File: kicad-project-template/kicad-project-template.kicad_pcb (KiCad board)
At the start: 2 copper layers, 25 x 25 mm, 1 part

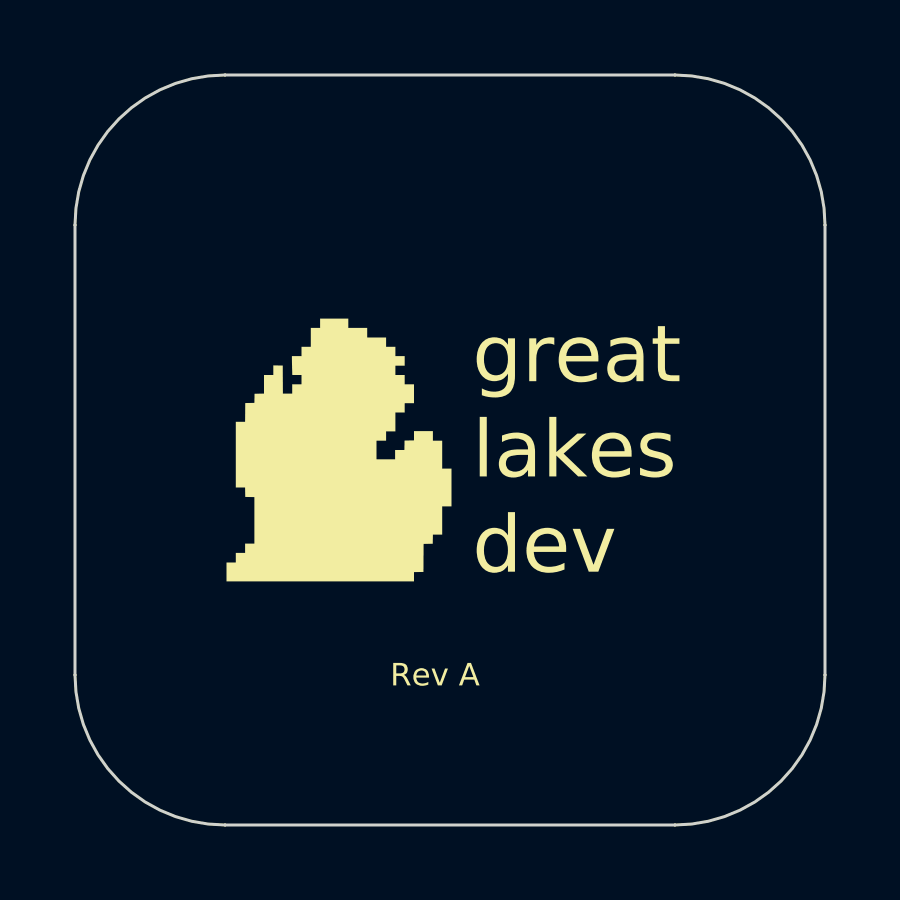
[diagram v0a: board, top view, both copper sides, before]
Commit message: Updated logos and sheet naming to everyday dev
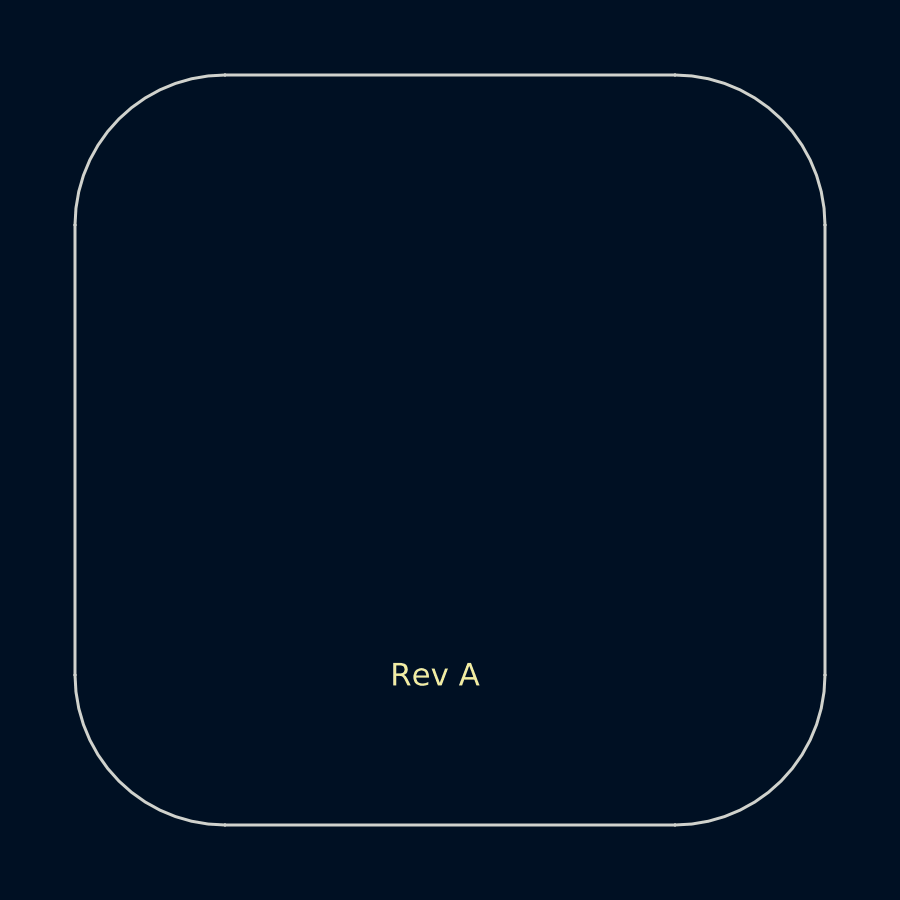
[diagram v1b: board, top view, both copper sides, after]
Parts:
- removed the G*** at (108.8, 97.5)
- added G***: LOGO, gld:edd-logo, F.Cu at (112.3, 96.9)

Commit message: Added manufacturer to bom output and updated MFP to MPN to follow other standards
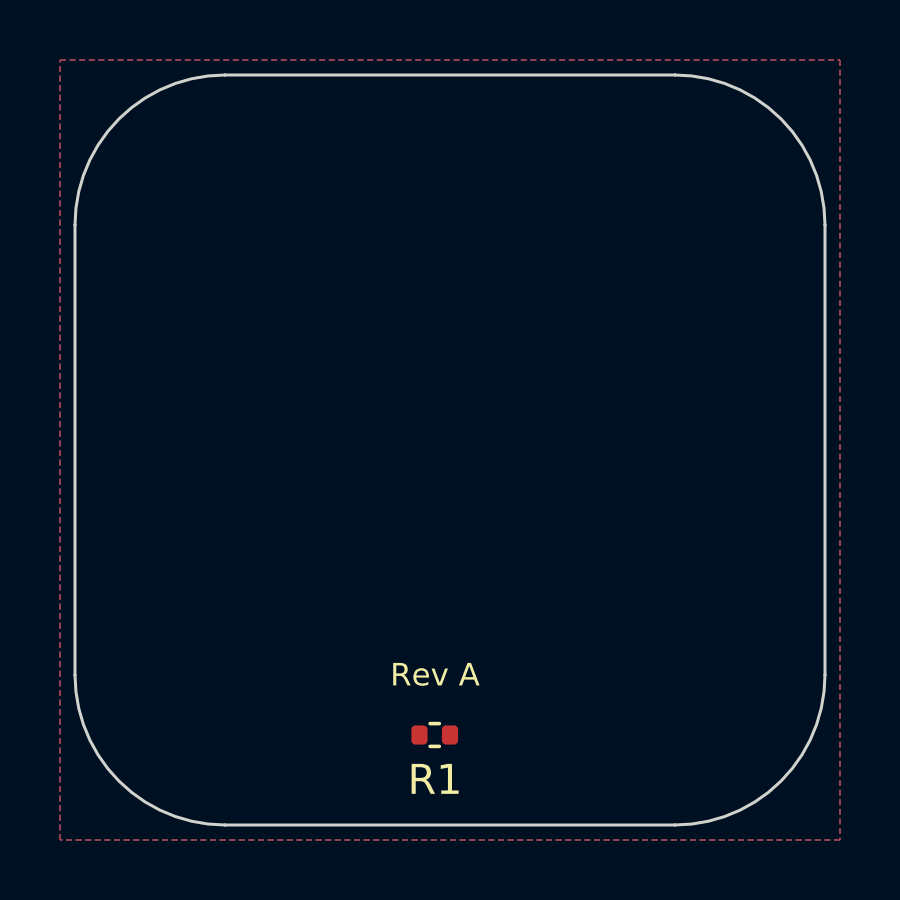
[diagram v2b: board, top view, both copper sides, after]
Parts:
- added R1: 10k, Resistor_SMD:R_0402_1005Metric, F.Cu at (112.0, 107.0)
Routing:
- added copper zone on B.Cu, net GND
- added copper zone on F.Cu, net GND
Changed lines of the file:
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@@
   )
   (net 0 "")
+  (net 1 "VCC")
+  (net 2 "GND")
   (footprint "gld:edd-logo" (layer "F.Cu")
     (at 112.3 96.9)
@@
       (stroke (width 0) (type solid)) (fill solid) (layer "F.Mask"))
   )
+  (footprint "Resistor_SMD:R_0402_1005Metric" (layer "F.Cu")
+    (at 111.99 107)
+    (descr "Resistor SMD 0402 (1005 Metric), square (rectangular) end terminal, IPC_7351 nominal, (Body size source: IPC-SM-782 page 72, https://www.pcb-3d.com/wordpress/wp-content/uploads/ipc-sm-782a_amendment_1_and_2.pdf), generated with kicad-footprint-generator")
+    (tags "resistor")
+    (property "MPN" "")
+    (property "Manufacturer" "")
+    (property "Sheetfile" "kicad-project-template.kicad_sch")
+    (property "Sheetname" "")
+    (property "ki_description" "Resistor, small US symbol")
+    (property "ki_keywords" "r resistor")
+    (attr smd)
+    (fp_text reference "R1" (at 0.01 1.5) (layer "F.SilkS")
+        (effects (font (size 1 1) (thickness 0.15)))
+    )
+    (fp_text value "10k" (at 0 1.17) (layer "F.Fab")
+        (effects (font (size 1 1) (thickness 0.15)))
+    )
+    (fp_text user "${REFERENCE}" (at 0 0) (layer "F.Fab")
+        (effects (font (size 0.26 0.26) (thickness 0.04)))
+    )
+    (fp_line (start -0.153641 -0.38) (end 0.153641 -0.38)
+      (stroke (width 0.12) (type solid)) (layer "F.SilkS"))
+    (fp_line (start -0.153641 0.38) (end 0.153641 0.38)
+      (stroke (width 0.12) (type solid)) (layer "F.SilkS"))
+    (fp_line (start -0.93 -0.47) (end 0.93 -0.47)
+      (stroke (width 0.05) (type solid)) (layer "F.CrtYd"))
+    (fp_line (start -0.93 0.47) (end -0.93 -0.47)
+      (stroke (width 0.05) (type solid)) (layer "F.CrtYd"))
+    (fp_line (start 0.93 -0.47) (end 0.93 0.47)
+      (stroke (width 0.05) (type solid)) (layer "F.CrtYd"))
+    (fp_line (start 0.93 0.47) (end -0.93 0.47)
+      (stroke (width 0.05) (type solid)) (layer "F.CrtYd"))
+    (fp_line (start -0.525 -0.27) (end 0.525 -0.27)
+      (stroke (width 0.1) (type solid)) (layer "F.Fab"))
+    (fp_line (start -0.525 0.27) (end -0.525 -0.27)
+      (stroke (width 0.1) (type solid)) (layer "F.Fab"))
+    (fp_line (start 0.525 -0.27) (end 0.525 0.27)
+      (stroke (width 0.1) (type solid)) (layer "F.Fab"))
+    (fp_line (start 0.525 0.27) (end -0.525 0.27)
+      (stroke (width 0.1) (type solid)) (layer "F.Fab"))
+    (pad "1" smd roundrect (at -0.51 0) (size 0.54 0.64) (layers "F.Cu" "F.Paste" "F.Mask") (roundrect_rratio 0.25)
+      (net 1 "VCC") (pintype "passive"))
+    (pad "2" smd roundrect (at 0.51 0) (size 0.54 0.64) (layers "F.Cu" "F.Paste" "F.Mask") (roundrect_rratio 0.25)
+      (net 2 "GND") (pintype "passive"))
+    (model "${KICAD6_3DMODEL_DIR}/Resistor_SMD.3dshapes/R_0402_1005Metric.wrl"
+      (offset (xyz 0 0 0))
+      (scale (xyz 1 1 1))
+      (rotate (xyz 0 0 0))
+    )
+  )
   (gr_arc (start 100 90) (mid 101.464466 86.464466) (end 105 85)
     (stroke (width 0.1) (type solid)) (layer "Edge.Cuts"))
@@
     (effects (font (size 0.75 0.75) (thickness 0.15)))
   )
+  (zone (net 2) (net_name "GND") (layers "F&B.Cu") (hatch edge 0.5)
+    (connect_pads (clearance 0.508))
+    (min_thickness 0.25) (filled_areas_thickness no)
+    (fill yes (thermal_gap 0.5) (thermal_bridge_width 0.5))
+    (polygon
+      (pts
+        (xy 99.5 110.5)
+        (xy 99.5 84.5)
+        (xy 125.5 84.5)
+        (xy 125.5 110.5)
+      )
+    )
+  )
 )
